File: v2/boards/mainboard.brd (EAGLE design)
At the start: 119.6 x 119.8 mm, 185 parts, among them IC1 LM2596S-ADJ, IC10 TSOP34830, IC11 DRV8835, IC12 ESP-WROOM-32, IC13 PAM8403, IC2 LM2596S-5.0, IC3 LD1117A, IC4 LM393, IC5 MCP101-300, IC6 TEENSY 3.6, IC7 PCA9634, IC8 PCA9554, IC9 PCA9634, J1 Bat_In, J10 SPI_0, J11 SPI_2, J12 SPI_2, J13 I2C_0, J14 I2C_1, J15 I2C_3, J16 BNO055, J17 Uart_2, J18 Uart_5, J19 Uart_6 (LP), J2 Erw_Pow, J20 BPS, J21 Servo_2, J22 Servo_3, J23 Erw_Servo, J24 Erw_PWM, J25 ESP32_Uart, J26 SPEAKER_L, J27 SPEAKER_R, J28 AUDIO_TEENSY, J29 SWD, J3 I2C0_5V, J30 SWD_KL02, J31 Erw_ENA, J32 Erw_GPIO, J33 Erw_analog, J34 USB_Host, J35 ESP32_PROG, J4 I2C3_5V, J5 Servo_1, J6 H-Bridge Mode, J7 RC5_SEL, J8 SPI_0, J9 SPI_0, SW1 TL32PO, U1 IRL3103, U4 BS108, U5 BS108, U6 BS108, U7 BS108, U8 BS108, U9 BS108, X1 max. 18V

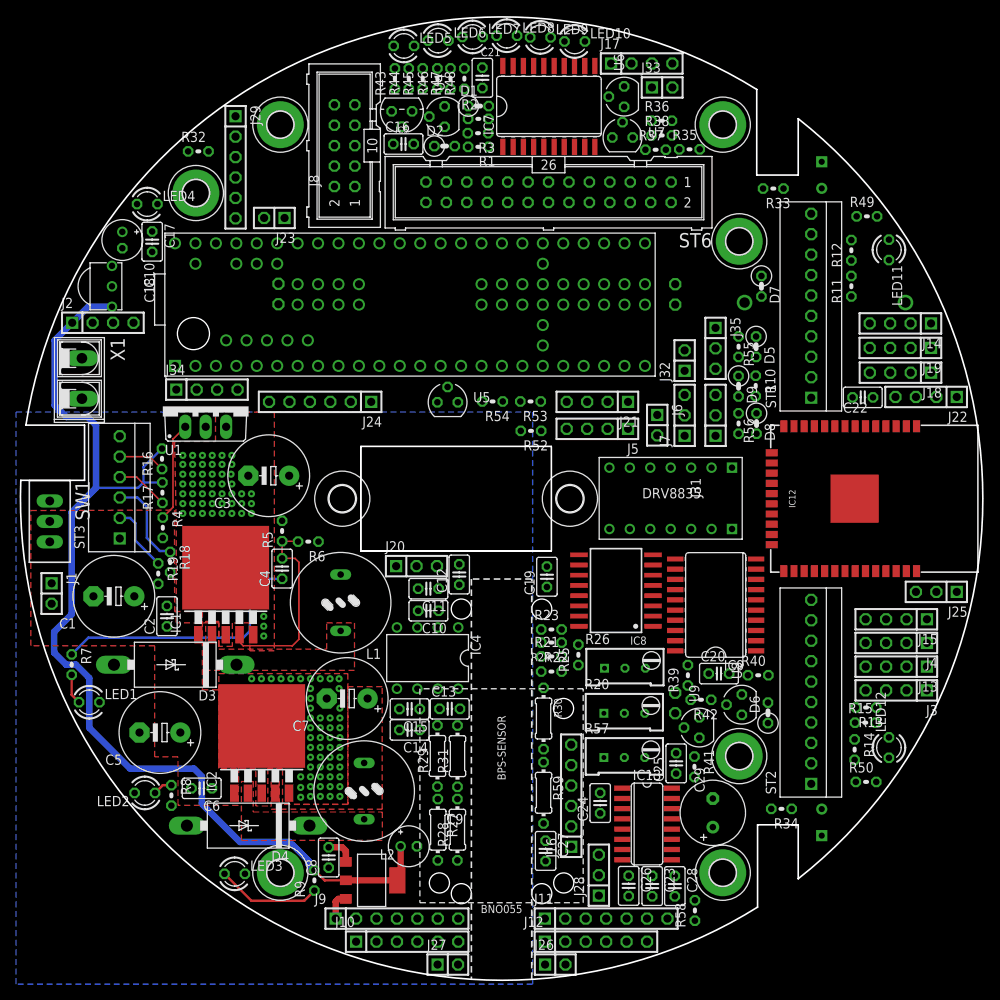
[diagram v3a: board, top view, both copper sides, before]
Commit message: ct-bot v2 schematic updated
- optional current measurements added to mainboard
 - schematic drafts for sensor boards
 - pin mapping sheet updated (i2c-bus mapping)
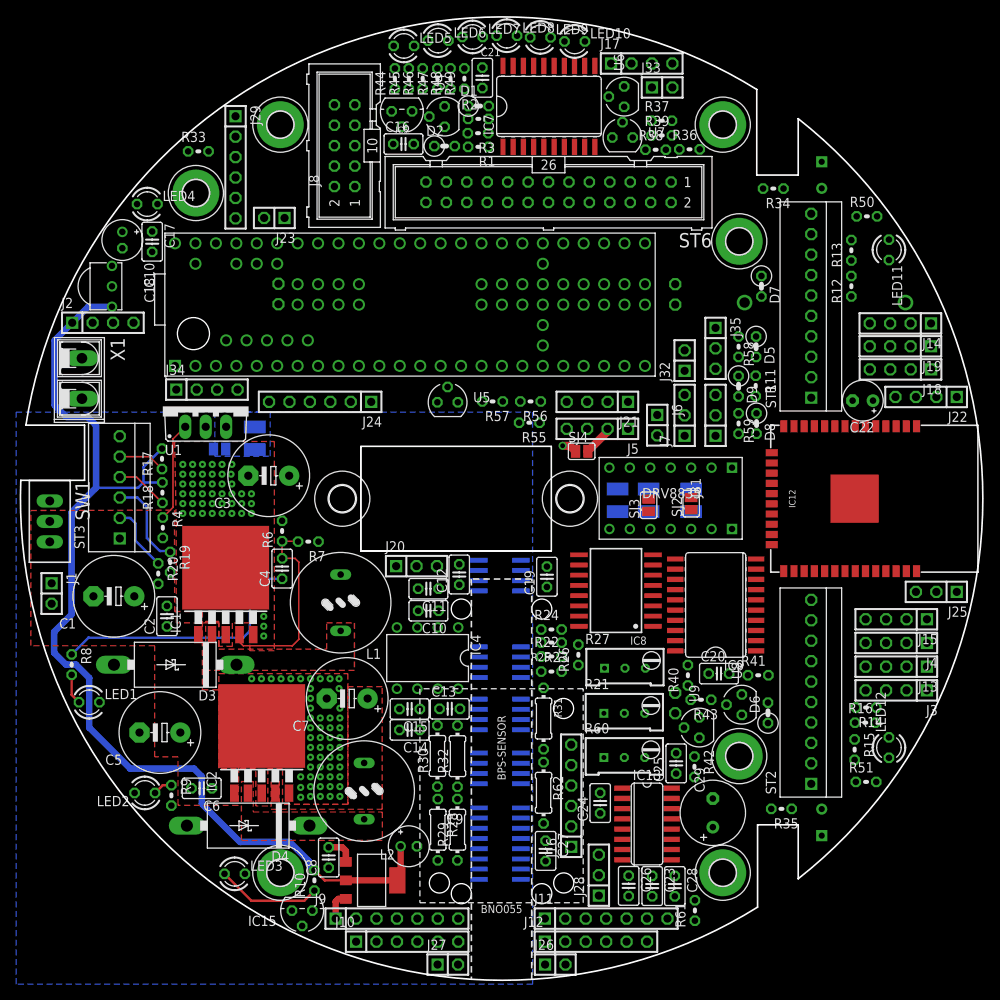
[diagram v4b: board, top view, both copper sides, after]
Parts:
- added IC15: MC1525, ct-bot:TO92
- added IC16, IC17, IC18, IC19: INA282, ct-bot:SO08
- added IC20: MCP3008, ct-bot:SO16
- added R51: 4k7, rcl:0204V
- added R60: 5k, ct-bot:RTRIM64W
- added R61: 10k, rcl:0204V
- added R62: 10k, rcl:0204/7
- added SJ1, SJ2, SJ3, SJ4: (no value), jumper:SJ
- C22: device rcl:C025-025X050 -> rcl:E2,5-5
- J2: value Erw_Pow -> Erw_Pwr
- R10: value 180 -> 120
- R12, R16: value 47k -> 180
- R14, R18: value 180 -> 47k
- R20: value 5k -> 180; device ct-bot:RTRIM64W -> rcl:0204V
- R21: value 10k -> 5k; device rcl:0204V -> ct-bot:RTRIM64W
- R22, R28: value 1M -> 10k
- R23, R29: value 10k -> 1M
- R25, R31: value 15k -> 10k
- R26: value 5k -> 15k; device ct-bot:RTRIM64W -> rcl:0204V
- R27: value 10k -> 5k; device rcl:0204/7 -> ct-bot:RTRIM64W
- R32: value 100 -> 15k; device rcl:0204V -> rcl:0204/7
- R33: value 470k -> 100
- R35: value 4k7 -> 470k
- R37, R55, R56: value 10k -> 4k7
- R39: value 1k1 -> 10k
- R41: value 1k8 -> 1k1
- R43, R49: value 4k7 -> 1k8
- R44: value 3k9 -> 4k7
- R45: value 220 -> 3k9
- R46: value 590 -> 220
- R47: value 115 -> 590
- R48: value 1k8 -> 115
- R5: value 3k9 0.1% -> 20m; device rcl:0204V -> rcl:R1210
- R52, R53, R54: value 4k7 -> 20m; device rcl:0204V -> rcl:R1210
- R57: value 5k -> 4k7; device ct-bot:RTRIM64W -> rcl:0204V
- R59: device rcl:0204/7 -> rcl:0204V
- R6: value 1k 0.1% -> 3k9 0.1%
- R7: value 390 -> 1k 0.1%
- R8: value 330 -> 390
- R9: value 120 -> 330
- moved R16 93.4 mm to (45.2, -27.8), turned to 0 degrees
- moved R43 86.1 mm to (24.8, -25.0), turned to 180 degrees
- moved R35 82.8 mm to (34.8, -38.6), turned to 180 degrees
- moved R10 82.4 mm to (-23.3, -47.4), turned to 90 degrees
- moved R32 81.8 mm to (-5.48, -32.0), turned to 90 degrees
- moved R34 77.1 mm to (33.8, 38.6)
- moved R33 71.6 mm to (-37.7, 43.2), turned to 0 degrees
- moved R50 70.3 mm to (45.4, 35.1)
- moved R58 70.3 mm to (29.5, 18.9), turned to 270 degrees
- moved R39 67.2 mm to (19.9, 45.2), turned to 0 degrees
- moved R20 60.4 mm to (-42.7, -9.31)
- moved R13 56.9 mm to (43.5, 30.9), turned to 90 degrees
- moved R49 52.9 mm to (-4.62, 52.2), turned to 90 degrees
- moved R59 51.9 mm to (29.5, 9.35)
- moved R57 46.8 mm to (-1.12, 12.1), turned to 180 degrees
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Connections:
- new net BAT_CUR: IC17.5, IC20.1
- new net GND_BAT: IC17.1, R5.2, SJ1.2, U1.S
- new net MCP_CH4: IC20.5
- new net MCP_CH5: IC20.6
- new net MCP_CH6: IC20.7
- new net MCP_CH7: IC20.8
- new net MOT_L_CUR: IC18.5, IC20.2
- new net MOT_L_SENS: IC18.1, R53.2, SJ3.2, ST5.2
- new net MOT_R_CUR: IC19.5, IC20.3
- new net MOT_R_SENS: IC19.1, R52.2, SJ2.2, ST4.2
- new net REF_2.5: IC15.2, IC18.3, IC19.3, IC20.15
- new net SERVO_CUR: IC16.5, IC20.4
- new net SERVO_PWR: IC16.1, J21.2, J22.2, J5.2, R54.2, SJ4.2, ST6.22
- net +3V3: now also C22.+, IC15.3, IC16.6, IC17.6, IC18.6, IC19.6, IC20.16, R10.2, R13.2, R14.1, R18.2, R21.3, R24.2, R26.2, R27.3, R30.2, R37.2, R41.2, R55.2, R57.2, R58.1, R59.2; no longer C22.1, R12.2, R13.1, R16.2, R20.3, R23.2, R25.2, R26.3, R29.2, R31.2, R39.2, R52.2, R53.2, R54.2, R55.1, R9.2
- net +5V: now also R39.2, R43.2, R51.1, R9.2; no longer R37.2, R41.2, R43.1, R8.2
- net +6V: now also IC16.8, R54.1, R6.2, R8.1, SJ4.1; no longer J21.2, J22.2, J5.2, R5.2, R7.1, ST6.22
- net DRV_KANTLED_L: now also R12.2; no longer R11.2
- net DRV_KANTLED_R: now also R16.1; no longer R15.1
- net DRV_LINE_L: now also R20.2; no longer R19.2
- net DRV_LINE_R: now also R19.2; no longer R18.2
- net DRV_RADLED_L: now also R11.2; no longer R10.2
- net DRV_RADLED_R: now also R15.1; no longer R14.1
- net EN: now also R59.1; no longer R56.1
- net ENC_L: now also R25.2, R26.1; no longer R24.2, R25.1
- net ENC_R: now also R31.2, R32.1; no longer R30.2, R31.1
- net GND: now also C22.-, IC15.1, IC16.2, IC16.3, IC16.7, IC17.2, IC17.3, IC17.7, IC17.8, IC18.2, IC18.7, IC19.2, IC19.7, IC20.14, IC20.9, R21.1, R27.1, R5.1, R60.3, R7.1, SJ1.1; no longer C22.2, R20.1, R26.1, R57.3, R6.1, U1.S
- net IO0: now also R58.2; no longer R55.2
- net KANTE_L: now also R13.1; no longer R12.1
- net KANTE_R: now also R14.2; no longer R13.2
- net LDR_L: now also R34.1; no longer R33.1
- net LDR_R: now also R35.1; no longer R34.1
- net LINE_IN_L: now also R60.1; no longer R57.1
- net LINIE_L: now also R18.1; no longer R17.1
- net LINIE_R: now also R17.1; no longer R16.1
- net MOT_L_2: now also IC18.8, R53.1, SJ3.1; no longer ST5.2
- net MOT_R_2: now also IC19.8, R52.1, SJ2.1; no longer ST4.2
- net N$1: now also R19.1; no longer R18.1
- net N$10: now also R31.1; no longer R30.1
- net N$11: now also R9.1; no longer R8.1
- net N$2: now also R10.1; no longer R9.1
- net N$20: now also R44.2; no longer R43.2
- net N$21: now also R45.2; no longer R44.2
- net N$22: now also R46.2; no longer R45.2
- net N$23: now also R47.2; no longer R46.2
- net N$24: now also R48.2; no longer R47.2
- net N$25: now also R49.2; no longer R48.2
- net N$26: now also R50.2; no longer R49.2
- net N$27: now also R51.2; no longer R50.2
- net N$28: now also R33.1; no longer R32.1
- net N$30: now also R20.1; no longer R19.1
- net N$34: now also R21.2, R22.1; no longer R20.2, R21.1
- net N$35: now also R22.2, R23.1; no longer R21.2, R22.1
- net N$36: now also R27.2, R28.1; no longer R26.2, R27.1
- net N$37: now also R28.2, R29.1; no longer R27.2, R28.1
- net N$40: now also R61.1; no longer R58.1
- net N$41: now also R61.2; no longer R58.2
- net N$42: now also R60.2; no longer R57.2
- net N$45: now also R15.2; no longer R14.2
- net N$46: now also R62.1; no longer R59.1
- net N$47: now also R11.1; no longer R10.1
- net N$48: now also R62.2; no longer R59.2
- net N$5: now also R25.1; no longer R24.1
- net N$51: now also R12.1; no longer R11.1
- net N$53: now also R16.2; no longer R15.2
- net N$8: now also R8.2; no longer R7.2
- net N$9: now also R6.1, R7.2; no longer R5.1, R6.2
- net RAD_L: now also R23.2, R24.1; no longer R22.2, R23.1
- net RAD_R: now also R29.2, R30.1; no longer R28.2, R29.1
- net SCL0: now also R37.1; no longer R36.1
- net SCL0_5V: now also R39.1; no longer R38.1
- net SCL3: now also R41.1; no longer R40.1
- net SCL3_5V: now also R43.1; no longer R42.1
- net SDA0: now also R36.1; no longer R35.1
- net SDA0_5V: now also R38.1; no longer R37.1
- net SDA3: now also R40.1; no longer R39.1
- net SDA3_5V: now also R42.1; no longer R41.1
- net SERVO1_PWM: now also R55.1; no longer R52.1
- net SERVO2_PWM: now also R56.1; no longer R53.1
- net SERVO3_PWM: now also R57.1; no longer R54.1
- net SERVO5_PWM: now also IC20.10
- net SPI0_MISO: now also IC20.12
- net SPI0_MOSI: now also IC20.11
- net SPI0_SCK: now also IC20.13
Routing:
- net +6V: track 140.5 -> 130.6 mm, vias 0 -> 1
- net SERVO_PWR: track 0.00 -> 7.17 mm
- net GND: vias 105 -> 99
- added copper zone on layer 16, net GND_BAT

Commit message: ct-bot v2 schematic updated according to todo list
- analog ground
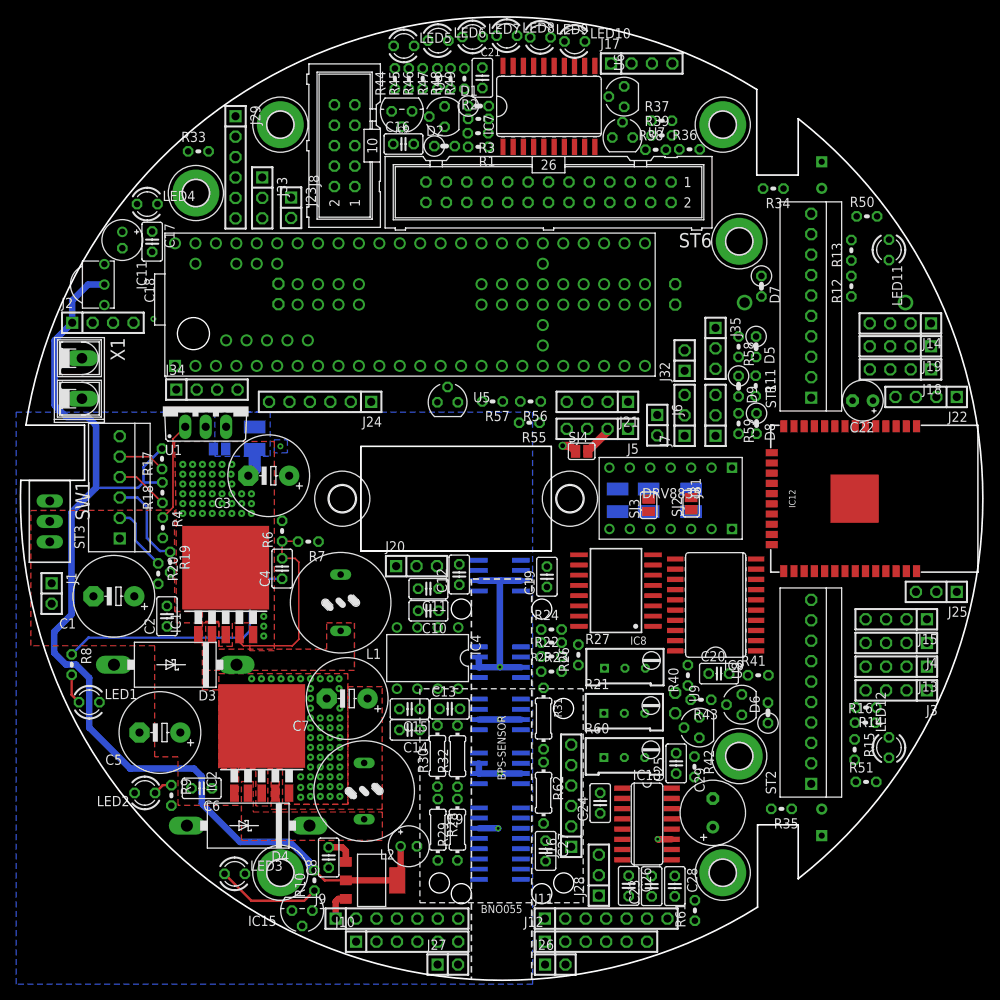
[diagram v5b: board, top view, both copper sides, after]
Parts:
- IC10: value TSOP34830 -> DRV8835; device ct-bot:TSOP348 -> ct-bot:DRV8835
- IC11: value DRV8835 -> TSOP324; device ct-bot:DRV8835 -> ct-bot:TSOP324
- J33: device ct-bot:1X02 -> ct-bot:1X03
- moved IC11 65.2 mm to (-49.4, 26.6)
- moved IC10 64.2 mm to (12.1, 5.13)
- moved J33 51.6 mm to (-29.7, 37.4), turned to 270 degrees
- moved J23 2.44 mm to (-26.2, 36.2), turned to 270 degrees
- moved C23 0.06 mm to (18.7, -48.2), turned to 90 degrees
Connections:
- new net AGND: C25.2, C26.2, IC13.11, IC15.1, IC16.2, IC16.3, IC16.7, IC17.2, IC17.3, IC17.7, IC18.2, IC18.7, IC19.2, IC19.7, IC20.14, IC6.AGND, J33.3, R60.3
- net +3V3: now also IC11.2; no longer IC10.3
- net +5V: now also IC10.VCC; no longer IC11.VCC
- net +6V: now also IC10.VIN; no longer IC11.VIN
- net FERNBED: now also IC11.1; no longer IC10.1
- net GND: now also IC10.LGND, IC10.MGND, IC11.3; no longer C25.2, C26.2, IC10.2, IC11.LGND, IC11.MGND, IC13.11, IC15.1, IC16.2, IC16.3, IC16.7, IC17.2, IC17.3, IC17.7, IC18.2, IC18.7, IC19.2, IC19.7, IC20.14, IC6.AGND, R60.3
- net MOT_L_1: now also IC10.AOUT1; no longer IC11.AOUT1
- net MOT_L_2: now also IC10.AOUT2; no longer IC11.AOUT2
- net MOT_L_DIR: now also IC10.APHASE; no longer IC11.APHASE
- net MOT_L_PWM: now also IC10.AENBL; no longer IC11.AENBL
- net MOT_R_1: now also IC10.BOUT1; no longer IC11.BOUT1
- net MOT_R_2: now also IC10.BOUT2; no longer IC11.BOUT2
- net MOT_R_DIR: now also IC10.BPHASE; no longer IC11.BPHASE
- net MOT_R_PWM: now also IC10.BENBL; no longer IC11.BENBL
- net N$3: now also IC10.MODE; no longer IC11.MODE
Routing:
- net AGND: track 0.00 -> 196.2 mm, vias 0 -> 7
- net GND: track 3.68 -> 7.27 mm
- net +3V3: track 132.1 -> 133.9 mm
- added copper zone on layer 15, net AGND
- added copper zone on layer 16, net AGND

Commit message: folder structure cleanup, 3d model: base updated
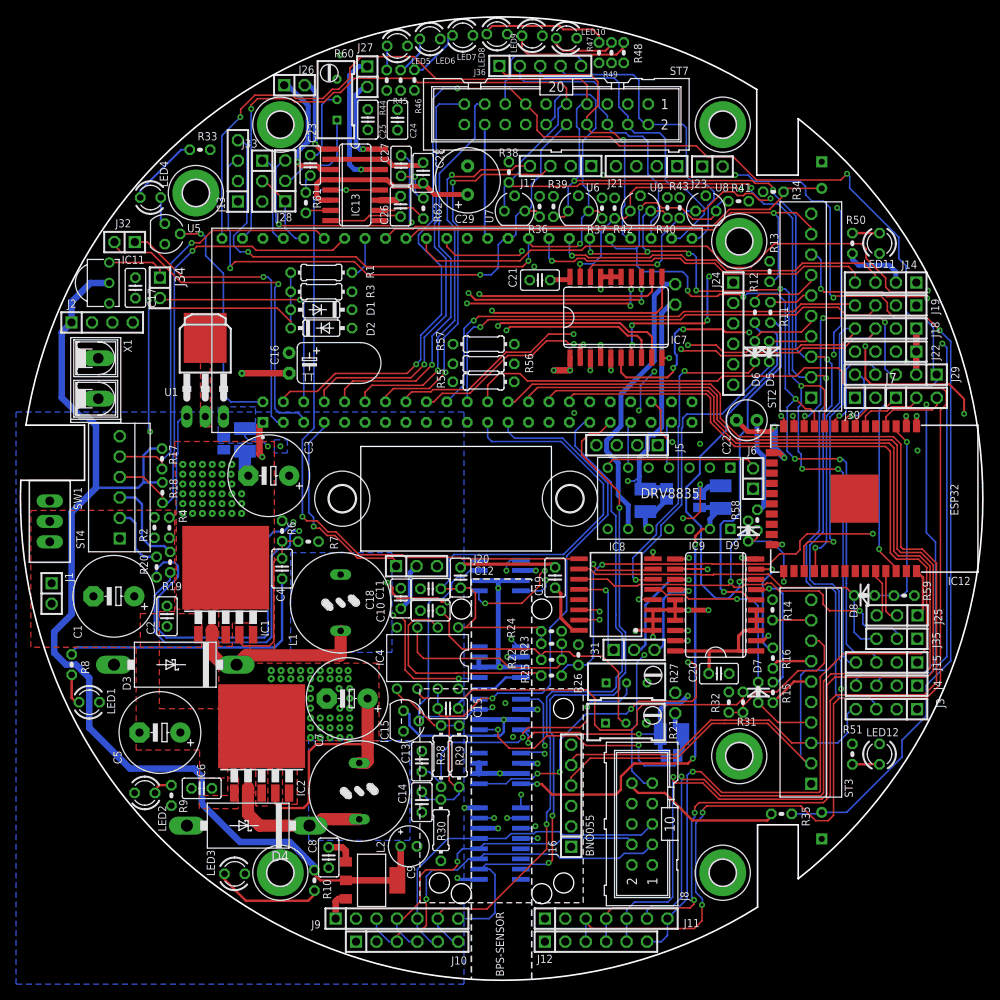
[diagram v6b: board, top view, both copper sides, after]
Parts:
- removed BT1: CR2032, ct-bot:00MM_PTH
- removed IC5: MCP101-300, ct-bot:TO-92
- removed IC6: TEENSY 3.6, ct-bot:T36
- removed U4: BS108, ct-bot:SOT54E
- added J36: SPI1, ct-bot:1X05
- added ST7: RPI_Interface, con-harting-ml:ML20
- C16: value 100nF -> 10uF; device rcl:C025-025X050 -> rcl:TT2D5L
- C18: value 220uF -> 100nF; device rcl:E2-5 -> rcl:C025-025X050
- D1, D2: value 1N4148 -> BAT42; device ct-bot:0207/2V -> ct-bot:DO35-7
- D5, D6, D7, D8, D9: value 1N4148 -> BAT42
- J29: device ct-bot:1X06 -> ct-bot:1X05
- J30: device ct-bot:1X02/90 -> ct-bot:1X02
- J34: value USB_Host -> RC5; device ct-bot:1X04 -> ct-bot:1X02
- J7: value RC5_SEL -> ESP32_GPIO
- R1, R3, R55, R56, R57: device rcl:0204V -> rcl:0204/7
- R31, R32, R62: device rcl:0204/7 -> rcl:0204V
- ST1: value Sensoren L -> CTBOT_MCU_BRD; device ct-bot:TS_PS25_10 -> ct-bot:DIP66
- ST2: value Sensoren R -> Sensoren L
- ST3: value Liniensensoren -> Sensoren R; device ct-bot:TS_PS25_6 -> ct-bot:TS_PS25_10
- ST4: value Motor R -> Liniensensoren; device ct-bot:1X02/90 -> ct-bot:TS_PS25_6
- ST5: value Motor L -> Motor R
- ST6: value RPI_Interface -> Motor L; device con-harting-ml:ML26 -> ct-bot:1X02/90
- U1: value IRL3103 -> IRLU024N; device ct-bot:TO220BV -> ct-bot:TO251AA
- moved J26 114.0 mm to (-25.7, 51.4)
- moved J27 110.8 mm to (-16.7, 52.5), turned to 270 degrees
- moved J13 102.5 mm to (-32.8, 40.8), turned to 90 degrees
- moved R61 100.4 mm to (-24.3, 36.8)
- moved C23 99.2 mm to (-23.8, 41.4)
- moved J28 94.7 mm to (-26.9, 39.5)
- moved C28 94.0 mm to (-9.75, 40.5), turned to 90 degrees
- moved J8 92.1 mm to (17.5, -40.4)
- moved ST3 91.2 mm to (38.5, -24.0)
- moved C26 89.1 mm to (-12.6, 36.3), turned to 90 degrees
- moved R60 89.0 mm to (-20.8, 49.6), turned to 0 degrees
- moved C25 88.7 mm to (-16.6, 47.1), turned to 270 degrees
- moved C24 88.6 mm to (-12.9, 47.1)
- moved IC13 87.3 mm to (-18.2, 39.0)
- moved C27 87.1 mm to (-12.5, 41.4), turned to 90 degrees
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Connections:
- removed net +5V: C17.1, C18.+, C19.1, C20.1, C21.1, C24.1, C25.1, C28.1, C29.+, C7.+, C8.1, IC10.VCC, IC13.13, IC13.4, IC13.6, IC2.4, IC3.VIN, IC6.VIN, IC7.1, IC7.20, IC7.3, IC7.5, IC8.16, IC9.1, IC9.20, IC9.3, IC9.4, IC9.5, J10.1, J11.2, J12.2, J13.2, J14.2, J15.2, J16.1, J17.2, J18.2, J19.2, J2.2, J3.2, J34.1, J4.2, J6.1, J8.1, J9.1, L2.2, R38.2, R39.2, R42.2, R43.2, R44.1, R45.1, R46.1, R47.1, R48.1, R49.1, R50.1, R51.1, R9.2, ST1.1, ST2.1, ST3.1, ST6.23, ST6.25
- removed net 3V3_TEENSY: C16.1, IC5.2, IC6.3V3(1), IC6.3V3(2), IC6.3V3(3), IC6.3V3(4), J29.1
- removed net GPIO_28: IC6.28, J7.3
- removed net N$39: IC5.1, U4.G
- removed net RC5_ESP32: IC12.37, J7.1
- removed net SERVO3_FB: ST6.14
- removed net TEENSY_LED: IC6.13, U5.G
- removed net USB1_D+: IC6.D+, J34.3
- removed net USB1_D-: IC6.D-, J34.2
- removed net VBAT_RTC: BT1.1, IC6.VBAT
- new net DEBUG_LED: ST1.23, U5.G
- new net RC5: IC11.1, J34.1
- new net VCC: C16.+, C19.1, C20.1, C21.1, C24.1, C25.1, C28.1, C29.+, C7.+, C8.1, IC10.VCC, IC13.13, IC13.4, IC13.6, IC2.4, IC3.VIN, IC7.1, IC7.20, IC7.3, IC7.5, IC8.16, IC9.1, IC9.20, IC9.3, IC9.4, IC9.5, J10.1, J11.2, J12.2, J13.2, J14.2, J15.2, J16.1, J17.2, J18.2, J19.2, J2.2, J3.2, J4.2, J6.1, J8.1, J9.1, L2.2, R38.2, R39.2, R42.2, R43.2, R44.1, R45.1, R46.1, R47.1, R48.1, R49.1, R50.1, R51.1, R9.2, ST1.1, ST2.1, ST3.1, ST4.1, ST7.5
- net +3V3: now also C17.1, C18.1, D1.C, ST7.3; no longer D1.2, ST6.1
- net A22_DAC1: now also ST1.48; no longer IC6.DAC1
- net ABST_SHDN_R: now also D7.2; no longer D6.2
- net AGND: now also D2.A, R3.1, ST1.47; no longer IC6.AGND
- net AUDIO_OUT: now also ST1.49; no longer IC6.DAC0
- net BAT-: now also U1.2, U1.4; no longer U1.D
- net BAT_IN_FB: now also ST1.52; no longer IC6.39
- net BPS: now also ST1.4; no longer IC6.42
- net ENC_L: now also ST2.8; no longer ST1.8
- net ENC_R: now also ST3.8; no longer ST2.8
- net FERNBED: now also J34.2, ST1.25; no longer IC11.1, J7.2
- net GND: now also C16.-, C18.2, J29.2, ST1.11, ST3.10, ST4.6, ST7.20; no longer BT1.2, C16.2, C18.-, D2.1, IC5.3, IC6.G0, IC6.G1, IC6.G2, IC6.G3, IC6.G4, IC6.G5, IC6.G6, J29.3, J34.4, R3.1, ST1.10, ST3.6, ST6.24, ST6.26, U4.S
- net GND_BAT: now also U1.3; no longer U1.S
- net GPIO_24: now also ST1.2; no longer IC6.24
- net GPIO_46: now also ST1.3; no longer IC6.46
- net IO34: now also J7.2
- net IO35: now also J7.1
- net IO36: now also J7.3
- net KANTE_L: now also ST1.54, ST2.9; no longer IC6.18, ST1.9
- net KANTE_R: now also ST1.55, ST3.9; no longer IC6.19, ST2.9
- net LDR_L: now also ST1.53; no longer IC6.49
- net LDR_R: now also ST1.56; no longer IC6.50
- net LINIE_L: now also ST1.51, ST4.4; no longer IC6.A10, ST3.4
- net LINIE_R: now also ST1.50, ST4.5; no longer IC6.A11, ST3.5
- net MOT_L_1: now also ST6.1; no longer ST5.1
- net MOT_L_DIR: now also ST1.19; no longer IC6.40
- net MOT_L_PWM: now also ST1.20; no longer IC6.35
- net MOT_L_SENS: now also ST6.2; no longer ST5.2
- net MOT_R_1: now also ST5.1; no longer ST4.1
- net MOT_R_DIR: now also ST1.21; no longer IC6.41
- net MOT_R_PWM: now also ST1.22; no longer IC6.36
- net MOT_R_SENS: now also ST5.2; no longer ST4.2
- net N$1: now also ST4.3; no longer ST3.3
- net N$30: now also ST4.2; no longer ST3.2
- net N$38: now also U1.1; no longer U1.G
- net N$4: now also D1.A, D2.C; no longer D1.1, D2.2
- net N$45: now also ST3.6; no longer ST2.6
- net N$47: now also ST2.6; no longer ST1.6
- net N$51: now also ST2.7; no longer ST1.7
- net N$53: now also ST3.7; no longer ST2.7
- net PWM_ERW_1: now also ST1.39; no longer IC6.16
- net PWM_ERW_2: now also ST1.40; no longer IC6.17
- net PWM_ERW_3: now also ST1.42; no longer IC6.30
- net PWM_ERW_4: now also ST1.41; no longer IC6.29
- net PWM_ERW_5: now also ST1.43; no longer IC6.4
- net PWM_ERW_6: now also ST1.44; no longer IC6.3
- net RAD_L: now also ST1.12; no longer IC6.43
- net RAD_R: now also ST1.13; no longer IC6.44
- net RESET: now also J29.1, ST1.24, ST7.13; no longer IC6.R, J29.2, ST6.12, U4.D
- net RPI_3V3: now also ST7.11; no longer ST6.11
- net RPI_SPI0_CE1: now also J36.5, ST7.15; no longer ST6.10
- net RX1: now also ST1.26, ST7.19; no longer IC6.27, ST6.15
- net RX2: now also ST1.28; no longer IC6.9
- net RX5: now also ST1.30; no longer IC6.34
- net RX6: now also ST1.32; no longer IC6.47
- net SCHRANKE_SHDN: now also D6.2; no longer D7.2
- net SCL0: now also ST1.60, ST7.12; no longer IC6.7, ST6.21
- net SCL0_5V: now also ST1.45, ST3.3, ST7.7; no longer ST1.3, ST6.9
- net SCL1: now also ST1.61; no longer IC6.37
- net SCL3: now also ST1.64; no longer IC6.57
- net SDA0: now also ST1.59, ST7.10; no longer IC6.8, ST6.19
- net SDA0_5V: now also ST1.46, ST3.2, ST7.9; no longer ST1.2, ST6.7
- net SDA1: now also ST1.62; no longer IC6.38
- net SDA3: now also ST1.63; no longer IC6.56
- net SERVO1_FB: now also ST1.57; no longer IC6.22
- net SERVO1_PWM: now also ST1.14; no longer IC6.5
- net SERVO2_FB: now also ST1.58, ST7.18; no longer IC6.23, ST6.20
- net SERVO2_PWM: now also ST1.15, ST7.16; no longer IC6.6, ST6.18
- net SERVO3_PWM: now also ST1.16, ST7.14; no longer IC6.25, ST6.16
- net SERVO4_PWM: now also J10.6, ST1.17; no longer IC6.20
- net SERVO5_PWM: now also ST1.18; no longer IC6.21, J10.6
- net SERVO_PWR: now also ST7.1; no longer ST6.22
- net SPI0_CS0: now also ST1.8; no longer IC6.2
- net SPI0_CS4: now also ST1.9; no longer IC6.15
- net SPI0_CS5: now also ST1.10; no longer IC6.45
- net SPI0_MISO: now also ST1.6; no longer IC6.12
- net SPI0_MOSI: now also ST1.5; no longer IC6.11
- net SPI0_SCK: now also ST1.7; no longer IC6.14
- net SPI1_CS0: now also J36.4, ST1.68, ST7.2; no longer IC6.31, ST6.8
- net SPI1_MISO: now also J36.2, ST1.66, ST7.6; no longer IC6.1, ST6.2
- net SPI1_MOSI: now also J36.1, ST1.65, ST7.8; no longer IC6.0, ST6.4
- net SPI1_SCK: now also J36.3, ST1.67, ST7.4; no longer IC6.32, ST6.6
- net SPI2_CS0: now also ST1.37; no longer IC6.55
- net SPI2_CS1: now also ST1.38; no longer IC6.54
- net SPI2_MISO: now also ST1.35; no longer IC6.51
- net SPI2_MOSI: now also ST1.34; no longer IC6.52
- net SPI2_SCK: now also ST1.36; no longer IC6.53
- net SWCLK: now also J29.4; no longer IC6.DC, J29.5
- net SWDIO: now also J29.5; no longer IC6.DD, J29.6
- net SWD_EN: now also J29.3; no longer IC6.DE, J29.4
- net TX1: now also ST1.27, ST7.17; no longer IC6.26, ST6.17
- net TX2: now also ST1.29; no longer IC6.10
- net TX5: now also ST1.31; no longer IC6.33
- net TX6: now also ST1.33; no longer IC6.48
- net VL53L0X_SHUT_L: now also ST2.4; no longer ST1.4
- net VL53L0X_SHUT_R: now also D7.1, ST3.4; no longer D6.1, ST2.4
- net VL6180X_SHDN: now also D6.1, ST2.5; no longer D7.1, ST1.5
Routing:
- net +3V3: track 133.9 -> 616.2 mm, vias 0 -> 7
- net SDA0_5V: track 0.00 -> 266.4 mm, vias 0 -> 4
- net SCL0_5V: track 0.00 -> 251.4 mm, vias 0 -> 6
- net SPI0_MOSI: track 0.00 -> 213.2 mm, vias 0 -> 1
- net SPI0_MISO: track 0.00 -> 208.2 mm, vias 0 -> 1
- net SPI0_SCK: track 0.00 -> 197.0 mm
- net SERVO_PWR: track 7.17 -> 194.6 mm, vias 0 -> 9
- net SPI2_MOSI: track 0.00 -> 178.0 mm, vias 0 -> 2
- net RESET: track 0.00 -> 174.8 mm, vias 0 -> 4
- net LDR_R: track 0.00 -> 159.7 mm, vias 0 -> 5
- net SPI2_MISO: track 0.00 -> 158.1 mm, vias 0 -> 2
- net SPI2_SCK: track 0.00 -> 156.7 mm, vias 0 -> 1
- net SPI0_CS0: track 0.00 -> 153.1 mm
- net SDA3_5V: track 0.00 -> 151.2 mm, vias 0 -> 4
- net SPI2_CS0: track 0.00 -> 147.0 mm, vias 0 -> 1
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- added copper zone on layer 2, net AGND
- added copper zone on layer 1, net BAT-
- added copper zone on layer 15, net KEEPOUT
- added copper zone on layer 16, net KEEPOUT
- added copper zone on layer 2, net KEEPOUT
- added copper zone on layer 15, net VCC
- removed copper zone on layer 1, net +5V
- removed copper zone on layer 15, net +5V
- removed copper zone on layer 15, net AGND
- removed copper zone on layer 1, net V5_L1
- removed copper zone on layer 1, net V6_L1
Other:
- board text added: "ESP32"
